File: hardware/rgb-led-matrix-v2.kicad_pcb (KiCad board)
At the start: 2 copper layers, 75 x 55 mm, 160 parts, among them J1 AKL_5_2, P1 CONN_01X02, P2 CON-SENSOR, Q1 2N7002P, U1 XMC1100-16, U2 DRILL, U3 DRILL, U4 DRILL, U5 DRILL

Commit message: updated pcb layout for ws2813b led
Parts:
- removed Fiducial_Mark (x4): VAL**, kicad-libraries:Fiducial_Mark
- removed G***: LOGO, kicad-libraries:Logo_CoMCU
- removed G***: LOGO, kicad-libraries:WEEE_7mm
- removed G***: Logo_31x31, kicad-libraries:Logo_31x31
- removed LED1, LED10, LED11, LED12, LED13, LED14, LED15, LED16, LED17, LED18, LED19, LED2, LED20, LED21, LED22, LED23, LED24, LED25, LED26, LED27, LED28, LED29, LED3, LED30, LED31, LED32, LED33, LED34, LED35, LED36, LED37, LED38, LED39, LED4, LED40, LED41, LED42, LED43, LED44, LED45, LED46, LED47, LED48, LED49, LED5, LED50, LED51, LED52, LED53, LED54, LED55, LED56, LED57, LED58, LED59, LED6, LED60, LED61, LED62, LED63, LED64, LED7, LED8, LED9: WS2812B_LED, kicad-libraries:WS2812B_LED
- removed VAL: CE_5mm, kicad-libraries:CE_5mm
- added U10: WS2813B, kicad-libraries:WS2813B, F.Cu at (153.3, 99.3)
- added U11: WS2813B, kicad-libraries:WS2813B, F.Cu at (132.3, 57.3)
- added U12: WS2813B, kicad-libraries:WS2813B, F.Cu at (132.3, 64.3)
- added U13: WS2813B, kicad-libraries:WS2813B, F.Cu at (153.3, 78.3)
- added U14: WS2813B, kicad-libraries:WS2813B, F.Cu at (174.3, 92.3)
- added U15: WS2813B, kicad-libraries:WS2813B, F.Cu at (160.3, 99.3)
- added U16: WS2813B, kicad-libraries:WS2813B, F.Cu at (139.3, 57.3)
- added U17: WS2813B, kicad-libraries:WS2813B, F.Cu at (125.3, 64.3)
- added U18: WS2813B, kicad-libraries:WS2813B, F.Cu at (146.3, 78.3)
- added U19: WS2813B, kicad-libraries:WS2813B, F.Cu at (167.3, 92.3)
- added U20: WS2813B, kicad-libraries:WS2813B, F.Cu at (167.3, 99.3)
- added U21: WS2813B, kicad-libraries:WS2813B, F.Cu at (146.3, 57.3)
- added U22: WS2813B, kicad-libraries:WS2813B, F.Cu at (125.3, 71.3)
- added U23: WS2813B, kicad-libraries:WS2813B, F.Cu at (139.3, 78.3)
- added U24: WS2813B, kicad-libraries:WS2813B, F.Cu at (160.3, 92.3)
- added U25: WS2813B, kicad-libraries:WS2813B, F.Cu at (174.3, 99.3)
- added U26: WS2813B, kicad-libraries:WS2813B, F.Cu at (153.3, 57.3)
- added U27: WS2813B, kicad-libraries:WS2813B, F.Cu at (132.3, 71.3)
- added U28: WS2813B, kicad-libraries:WS2813B, F.Cu at (132.3, 78.3)
- added U29: WS2813B, kicad-libraries:WS2813B, F.Cu at (153.3, 92.3)
- added U30: WS2813B, kicad-libraries:WS2813B, F.Cu at (174.3, 106.3)
- added U31: WS2813B, kicad-libraries:WS2813B, F.Cu at (160.3, 57.3)
- added U32: WS2813B, kicad-libraries:WS2813B, F.Cu at (139.3, 71.3)
- added U33: WS2813B, kicad-libraries:WS2813B, F.Cu at (125.3, 78.3)
- added U34: WS2813B, kicad-libraries:WS2813B, F.Cu at (146.3, 92.3)
- added U35: WS2813B, kicad-libraries:WS2813B, F.Cu at (167.3, 106.3)
- added U36: WS2813B, kicad-libraries:WS2813B, F.Cu at (167.3, 57.3)
- added U37: WS2813B, kicad-libraries:WS2813B, F.Cu at (146.3, 71.3)
- added U38: WS2813B, kicad-libraries:WS2813B, F.Cu at (125.3, 85.3)
- added U39: WS2813B, kicad-libraries:WS2813B, F.Cu at (139.3, 92.3)
- added U40: WS2813B, kicad-libraries:WS2813B, F.Cu at (160.3, 106.3)
- added U41: WS2813B, kicad-libraries:WS2813B, F.Cu at (174.3, 57.3)
- added U42: WS2813B, kicad-libraries:WS2813B, F.Cu at (153.3, 71.3)
- added U43: WS2813B, kicad-libraries:WS2813B, F.Cu at (132.3, 85.3)
- added U44: WS2813B, kicad-libraries:WS2813B, F.Cu at (132.3, 92.3)
- added U45: WS2813B, kicad-libraries:WS2813B, F.Cu at (153.3, 106.3)
- added U46: WS2813B, kicad-libraries:WS2813B, F.Cu at (174.3, 64.3)
- added U47: WS2813B, kicad-libraries:WS2813B, F.Cu at (160.3, 71.3)
- added U48: WS2813B, kicad-libraries:WS2813B, F.Cu at (139.3, 85.3)
- added U49: WS2813B, kicad-libraries:WS2813B, F.Cu at (125.3, 92.3)
- added U50: WS2813B, kicad-libraries:WS2813B, F.Cu at (146.3, 106.3)
- added U51: WS2813B, kicad-libraries:WS2813B, F.Cu at (167.3, 64.3)
- added U52: WS2813B, kicad-libraries:WS2813B, F.Cu at (167.3, 71.3)
- added U53: WS2813B, kicad-libraries:WS2813B, F.Cu at (146.3, 85.3)
- added U54: WS2813B, kicad-libraries:WS2813B, F.Cu at (125.3, 99.3)
- added U55: WS2813B, kicad-libraries:WS2813B, F.Cu at (139.3, 106.3)
- added U56: WS2813B, kicad-libraries:WS2813B, F.Cu at (160.3, 64.3)
- added U57: WS2813B, kicad-libraries:WS2813B, F.Cu at (174.3, 71.3)
- added U58: WS2813B, kicad-libraries:WS2813B, F.Cu at (153.3, 85.3)
- added U59: WS2813B, kicad-libraries:WS2813B, F.Cu at (132.3, 99.3)
- added U6: WS2813B, kicad-libraries:WS2813B, F.Cu at (125.3, 57.3)
- added U60: WS2813B, kicad-libraries:WS2813B, F.Cu at (132.3, 106.3)
- added U61: WS2813B, kicad-libraries:WS2813B, F.Cu at (153.3, 64.3)
- added U62: WS2813B, kicad-libraries:WS2813B, F.Cu at (174.3, 78.3)
- added U63: WS2813B, kicad-libraries:WS2813B, F.Cu at (160.3, 85.3)
- added U64: WS2813B, kicad-libraries:WS2813B, F.Cu at (139.3, 99.3)
- added U65: WS2813B, kicad-libraries:WS2813B, F.Cu at (125.3, 106.3)
- added U66: WS2813B, kicad-libraries:WS2813B, F.Cu at (146.3, 64.3)
- added U67: WS2813B, kicad-libraries:WS2813B, F.Cu at (167.3, 78.3)
- added U68: WS2813B, kicad-libraries:WS2813B, F.Cu at (167.3, 85.3)
- added U69: WS2813B, kicad-libraries:WS2813B, F.Cu at (146.3, 99.3)
- added U7: WS2813B, kicad-libraries:WS2813B, F.Cu at (139.3, 64.3)
- added U8: WS2813B, kicad-libraries:WS2813B, F.Cu at (160.3, 78.3)
- added U9: WS2813B, kicad-libraries:WS2813B, F.Cu at (174.3, 85.3)
- moved R4 0.71 mm to (120.9, 58.8), turned to 270 degrees
- moved C20 0.11 mm to (176.0, 74.8), turned to 0 degrees
- moved C21 0.11 mm to (169.0, 74.8), turned to 0 degrees
- moved C22 0.11 mm to (162.0, 74.8), turned to 0 degrees
- moved C23 0.11 mm to (155.0, 74.8), turned to 0 degrees
- moved C24 0.11 mm to (148.0, 74.8), turned to 0 degrees
- moved C25 0.11 mm to (141.0, 74.8), turned to 0 degrees
- moved C26 0.11 mm to (134.0, 74.8), turned to 0 degrees
- moved C29 0.11 mm to (130.5, 74.8), turned to 180 degrees
- moved C30 0.11 mm to (137.5, 74.8), turned to 180 degrees
- moved C31 0.11 mm to (144.5, 74.8), turned to 180 degrees
- moved C32 0.11 mm to (151.5, 74.8), turned to 180 degrees
- moved C33 0.11 mm to (158.5, 74.8), turned to 180 degrees
- moved C34 0.11 mm to (165.5, 74.8), turned to 180 degrees
- moved C35 0.11 mm to (172.5, 74.8), turned to 180 degrees
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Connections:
- C10 pad 1: VCC -> GND
- C10 pad 2: GND -> VCC
- C11 pad 1: VCC -> GND
- C11 pad 2: GND -> VCC
- C12 pad 1: VCC -> GND
- C12 pad 2: GND -> VCC
- C13 pad 1: VCC -> GND
- C13 pad 2: GND -> VCC
- C14 pad 1: VCC -> GND
- C14 pad 2: GND -> VCC
- C15 pad 1: VCC -> GND
- C15 pad 2: GND -> VCC
- C16 pad 1: VCC -> GND
- C16 pad 2: GND -> VCC
- C17 pad 1: VCC -> GND
- C17 pad 2: GND -> VCC
- C18 pad 1: VCC -> GND
- C18 pad 2: GND -> VCC
- C19 pad 1: VCC -> GND
- C19 pad 2: GND -> VCC
- C20 pad 1: VCC -> GND
- C20 pad 2: GND -> VCC
- C21 pad 1: VCC -> GND
- C21 pad 2: GND -> VCC
- C22 pad 1: VCC -> GND
- C22 pad 2: GND -> VCC
- C23 pad 1: VCC -> GND
- C23 pad 2: GND -> VCC
- C24 pad 1: VCC -> GND
- C24 pad 2: GND -> VCC
- C25 pad 1: VCC -> GND
- C25 pad 2: GND -> VCC
- C26 pad 1: VCC -> GND
- C26 pad 2: GND -> VCC
- C27 pad 1: VCC -> GND
- C27 pad 2: GND -> VCC
- C28 pad 1: VCC -> GND
- C28 pad 2: GND -> VCC
- C29 pad 1: VCC -> GND
- C29 pad 2: GND -> VCC
- C30 pad 1: VCC -> GND
- C30 pad 2: GND -> VCC
- C31 pad 1: VCC -> GND
- C31 pad 2: GND -> VCC
- C32 pad 1: VCC -> GND
- C32 pad 2: GND -> VCC
- C33 pad 1: VCC -> GND
- C33 pad 2: GND -> VCC
- C34 pad 1: VCC -> GND
- C34 pad 2: GND -> VCC
- C35 pad 1: VCC -> GND
- C35 pad 2: GND -> VCC
- C36 pad 1: VCC -> GND
- C36 pad 2: GND -> VCC
- C37 pad 1: VCC -> GND
- C37 pad 2: GND -> VCC
- C38 pad 1: VCC -> GND
- C38 pad 2: GND -> VCC
- C39 pad 1: VCC -> GND
- C39 pad 2: GND -> VCC
- C40 pad 1: VCC -> GND
- C40 pad 2: GND -> VCC
- C41 pad 1: VCC -> GND
- C41 pad 2: GND -> VCC
- C42 pad 1: VCC -> GND
- C42 pad 2: GND -> VCC
- C43 pad 1: VCC -> GND
- C43 pad 2: GND -> VCC
- C44 pad 1: VCC -> GND
- C44 pad 2: GND -> VCC
- C45 pad 1: VCC -> GND
- C45 pad 2: GND -> VCC
- C46 pad 1: VCC -> GND
- C46 pad 2: GND -> VCC
- C47 pad 1: VCC -> GND
- C47 pad 2: GND -> VCC
- C48 pad 1: VCC -> GND
- C48 pad 2: GND -> VCC
- C49 pad 1: VCC -> GND
- C49 pad 2: GND -> VCC
- C50 pad 1: VCC -> GND
- C50 pad 2: GND -> VCC
- C51 pad 1: VCC -> GND
- C51 pad 2: GND -> VCC
- C52 pad 1: VCC -> GND
- C52 pad 2: GND -> VCC
- C53 pad 1: VCC -> GND
- C53 pad 2: GND -> VCC
- C54 pad 1: VCC -> GND
- C54 pad 2: GND -> VCC
- C55 pad 1: VCC -> GND
- C55 pad 2: GND -> VCC
- C56 pad 1: VCC -> GND
- C56 pad 2: GND -> VCC
- C57 pad 1: VCC -> GND
- C57 pad 2: GND -> VCC
- C58 pad 1: VCC -> GND
- C58 pad 2: GND -> VCC
- C59 pad 1: VCC -> GND
- C59 pad 2: GND -> VCC
- C6 pad 1: VCC -> GND
- C6 pad 2: GND -> VCC
- C60 pad 1: VCC -> GND
- C60 pad 2: GND -> VCC
- C61 pad 1: VCC -> GND
- C61 pad 2: GND -> VCC
- C62 pad 1: VCC -> GND
- C62 pad 2: GND -> VCC
- C63 pad 1: VCC -> GND
- C63 pad 2: GND -> VCC
- C64 pad 1: VCC -> GND
- C64 pad 2: GND -> VCC
- C65 pad 1: VCC -> GND
- C65 pad 2: GND -> VCC
- C66 pad 1: VCC -> GND
- C66 pad 2: GND -> VCC
- C67 pad 1: VCC -> GND
- C67 pad 2: GND -> VCC
- C68 pad 1: VCC -> GND
- C68 pad 2: GND -> VCC
- C69 pad 1: VCC -> GND
- C69 pad 2: GND -> VCC
- C7 pad 1: VCC -> GND
- C7 pad 2: GND -> VCC
- C8 pad 1: VCC -> GND
- C8 pad 2: GND -> VCC
- C9 pad 1: VCC -> GND
- C9 pad 2: GND -> VCC
- P2 pad 1: Net-(P2-Pad1) -> (no net)
- R2 pad 1: Net-(R2-Pad1) -> Net-(Q1-PadD)
- R3 pad 1: Net-(R3-Pad1) -> Net-(Q1-PadG)
- R4 pad 2: Net-(R2-Pad1) -> Net-(Q1-PadD)
- U1 pad 11: Net-(U1-Pad11) -> (no net)
- U1 pad 12: Net-(U1-Pad12) -> (no net)
- U1 pad 13: Net-(U1-Pad13) -> (no net)
- U1 pad 14: Net-(U1-Pad14) -> (no net)
- U1 pad 16: Net-(U1-Pad16) -> (no net)
- U1 pad 17: Net-(U1-Pad17) -> (no net)
- U1 pad 19: Net-(U1-Pad19) -> (no net)
- U1 pad 2: Net-(U1-Pad2) -> (no net)
- U1 pad 20: Net-(U1-Pad20) -> (no net)
- U1 pad 21: Net-(U1-Pad21) -> (no net)
- U1 pad 4: Net-(U1-Pad4) -> (no net)
- U1 pad 5: Net-(U1-Pad5) -> (no net)
- U1 pad 6: Net-(U1-Pad6) -> (no net)
- U1 pad 8: Net-(U1-Pad8) -> (no net)
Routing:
- net GND: track 1871.3 -> 547.4 mm, vias 2465 -> 993
- net (no net): track 0.00 -> 177.6 mm, vias 0 -> 96
- net VCC: track 537.6 -> 457.8 mm, vias 46 -> 78
- net Net-(U41-Pad3): track 0.00 -> 22.5 mm
- net Net-(U57-Pad3): track 0.00 -> 22.0 mm
- net Net-(U25-Pad3): track 0.00 -> 22.0 mm
- net Net-(U14-Pad4): track 0.00 -> 22.0 mm
- net Net-(U28-Pad3): track 0.00 -> 17.1 mm
- net Net-(U12-Pad3): track 0.00 -> 17.1 mm
- net Net-(U52-Pad3): track 0.00 -> 16.8 mm
- net Net-(U36-Pad3): track 0.00 -> 16.0 mm
- net Net-(U20-Pad3): track 0.00 -> 15.8 mm
- net Net-(U14-Pad6): track 0.00 -> 15.8 mm
- net Net-(U44-Pad3): track 0.00 -> 15.0 mm
- net Net-(U33-Pad3): track 0.00 -> 13.0 mm
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- removed copper zone on B.Cu, net VCC
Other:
- board text added: "RGB LED Matrix 2.0"
- board text removed: "RGB LED Matrix 1.0"

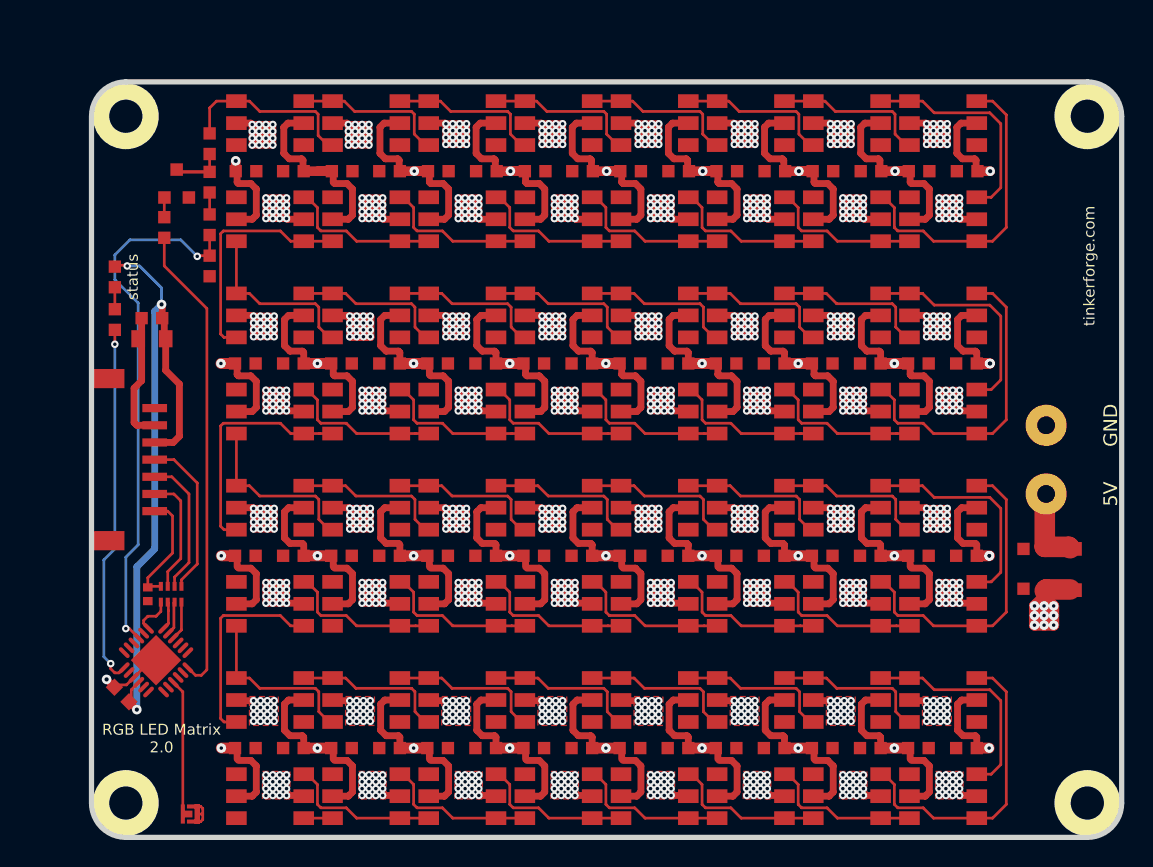
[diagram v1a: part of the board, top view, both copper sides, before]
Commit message: routing powerlanes on backside
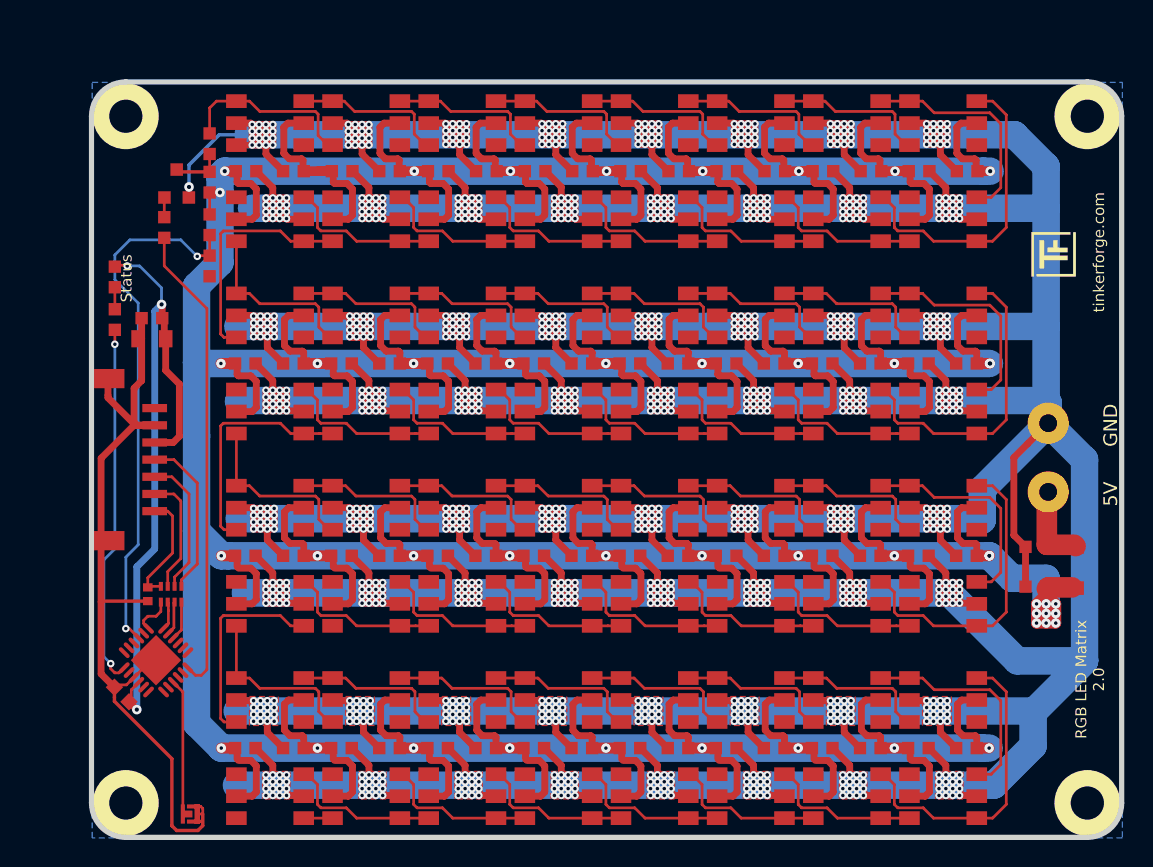
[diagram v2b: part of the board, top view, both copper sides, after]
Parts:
- added G***: LOGO, kicad-libraries:Logo_31x31, F.Cu at (182.3, 66.8)
- moved C4 0.21 mm to (181.1, 91.0)
- moved C5 0.21 mm to (181.1, 88.2)
- moved FB2 0.21 mm to (183.8, 89.7)
- moved J1 0.21 mm to (181.9, 81.7)
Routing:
- net GND: track 547.4 -> 1298.5 mm, vias 993 -> 1025
- net VCC: track 457.8 -> 738.3 mm, vias 78 -> 47
- added copper zone on B.Cu, net GND
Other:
- board text added: "Status"
- board text removed: "status"

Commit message: changed pcb layout
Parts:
- added Fiducial_Mark: VAL**, kicad-libraries:Fiducial_Mark, F.Cu at (114.3, 61.3)
- added Fiducial_Mark: VAL**, kicad-libraries:Fiducial_Mark, F.Cu at (181.3, 102.3)
- added Fiducial_Mark: VAL**, kicad-libraries:Fiducial_Mark, F.Cu at (181.3, 61.3)
- added Fiducial_Mark: VAL**, kicad-libraries:Fiducial_Mark, F.Cu at (114.3, 102.3)
- added G***: LOGO, kicad-libraries:Logo_CoMCU, B.Cu at (157.3, 81.8)
- added VAL: WEEE_7mm, kicad-libraries:WEEE_7mm, B.Cu at (149.8, 81.8)
- added VAL: CE_5mm, kicad-libraries:CE_5mm, B.Cu at (142.8, 81.8)
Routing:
- net (no net): track 177.6 -> 0.00 mm, vias 96 -> 0
- net GND: track 1298.5 -> 1302.1 mm, vias 1025 -> 1026
- net Net-(U44-Pad3): track 15.0 -> 17.1 mm
- net VCC: vias 47 -> 48

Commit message: final pcb design
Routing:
- net GND: track 1302.1 -> 1258.3 mm, vias 1026 -> 1034
- net 3V3: track 50.1 -> 50.0 mm, vias 3 -> 2

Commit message: corrected Fab.Layer
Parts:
- ?: renamed from G***; value LOGO -> (none)

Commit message: pcb design
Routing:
- net GND: track 1258.3 -> 1261.2 mm
- net VIN: track 38.9 -> 38.1 mm
- removed copper zone on F.Cu, net GND
